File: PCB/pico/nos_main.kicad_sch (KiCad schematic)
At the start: 159 parts, among them U1 PiPico_No_SWD, U2 ADG732BSUZ, U3 DC/DC

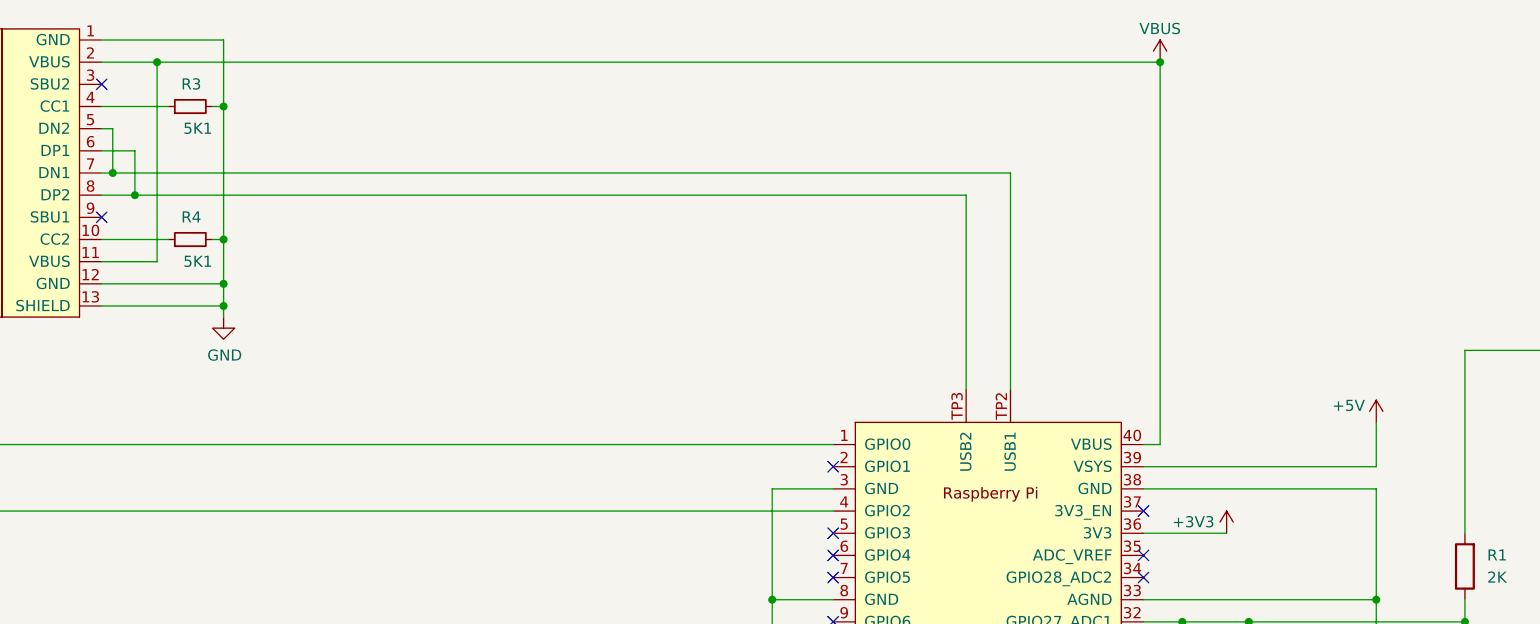
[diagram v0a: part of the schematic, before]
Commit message: Nos Pico PCB v1.12 (isolate vbus)
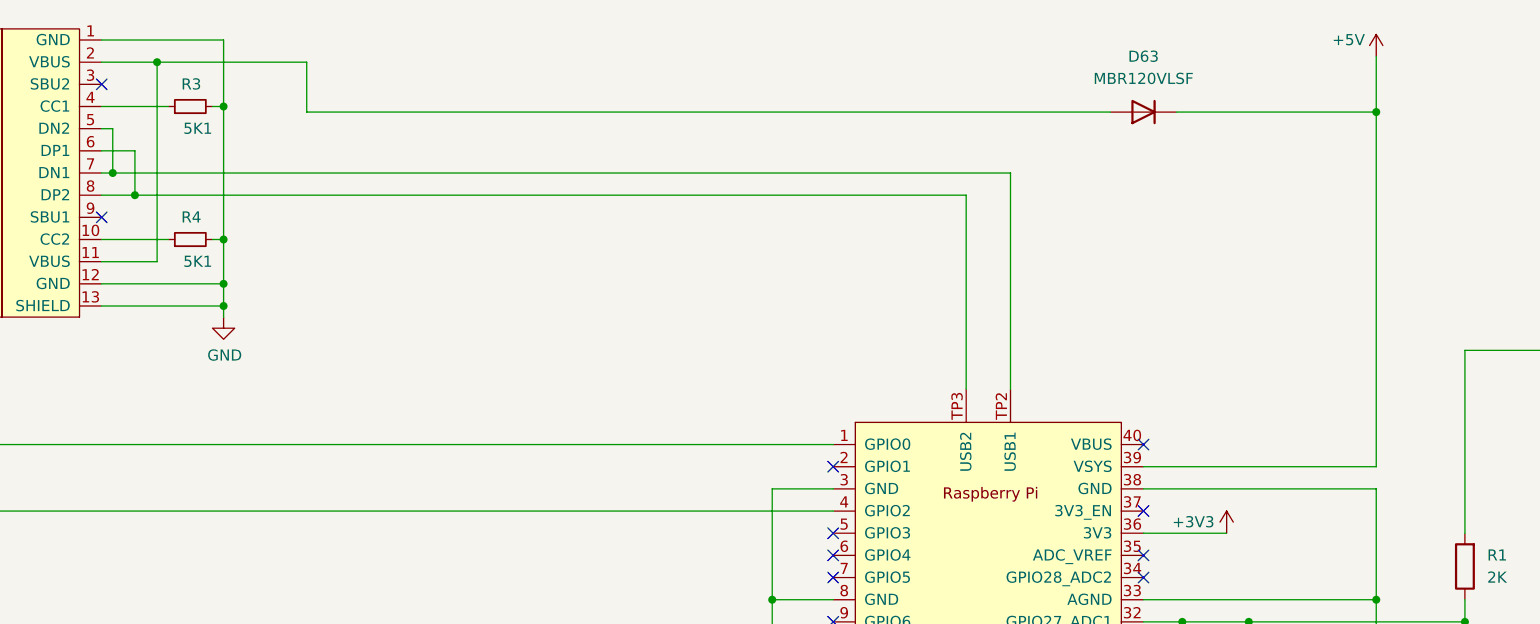
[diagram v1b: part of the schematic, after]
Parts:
- added D63: MBR120VLSF, Diode_SMD:D_SOD-123, symbol Device:D
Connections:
- net +5V: now also D63.1 (K)
- net VBUS: no longer names the net of USB1.11 (VBUS), USB1.2 (VBUS)
- net VBUS: now also D63.2 (A); no longer U1.40 (VBUS)
- no-connect marks 18 -> 19
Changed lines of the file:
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@@
 	)
 	(junction
+		(at 68.58 32.385)
+		(diameter 0)
+		(color 0 0 0 0)
+	)
+	(junction
 		(at 290.195 266.7)
 		(diameter 0)
@@
 	)
 	(junction
+		(at 208.28 38.1)
+		(diameter 0)
+		(color 0 0 0 0)
+	)
+	(junction
 		(at 381 235.585)
 		(diameter 0)
@@
 	)
 	(junction
-		(at 68.58 32.385)
-		(diameter 0)
-		(color 0 0 0 0)
-	)
-	(junction
 		(at 125.095 193.04)
 		(diameter 0)
@@
 	)
 	(junction
-		(at 183.515 32.385)
-		(diameter 0)
-		(color 0 0 0 0)
-	)
-	(junction
 		(at 74.295 215.9)
 		(diameter 0)
@@
 	)
 	(no_connect
+		(at 181.61 76.2)
+	)
+	(no_connect
 		(at 146.05 86.36)
 	)
@@
 	(wire
 		(pts
-			(xy 68.58 32.385) (xy 183.515 32.385)
-		)
-		(stroke
-			(width 0)
-			(type default)
-		)
-	)
-	(wire
-		(pts
 			(xy 407.035 266.7) (xy 419.735 266.7)
 		)
@@
 	(wire
 		(pts
+			(xy 208.28 38.1) (xy 208.28 78.74)
+		)
+		(stroke
+			(width 0)
+			(type default)
+		)
+	)
+	(wire
+		(pts
 			(xy 48.895 215.9) (xy 61.595 215.9)
 		)
@@
 	(wire
 		(pts
-			(xy 183.515 32.385) (xy 183.515 76.2)
-		)
-		(stroke
-			(width 0)
-			(type default)
-		)
-	)
-	(wire
-		(pts
 			(xy 137.795 165.735) (xy 150.495 165.735)
 		)
@@
 	(wire
 		(pts
-			(xy 208.28 73.66) (xy 208.28 78.74)
+			(xy 208.28 31.75) (xy 208.28 38.1)
 		)
 		(stroke
@@
 	(wire
 		(pts
-			(xy 400.05 235.585) (xy 413.385 235.585)
+			(xy 177.8 38.1) (xy 85.725 38.1)
 		)
 		(stroke
@@
 	(wire
 		(pts
-			(xy 353.695 266.7) (xy 368.935 266.7)
+			(xy 400.05 235.585) (xy 413.385 235.585)
 		)
 		(stroke
@@
 	(wire
 		(pts
-			(xy 381 235.585) (xy 400.05 235.585)
+			(xy 353.695 266.7) (xy 368.935 266.7)
 		)
 		(stroke
@@
 	(wire
 		(pts
-			(xy 62.23 40.005) (xy 63.5 40.005)
+			(xy 381 235.585) (xy 400.05 235.585)
 		)
 		(stroke
@@
 	(wire
 		(pts
-			(xy 290.195 266.7) (xy 302.895 266.7)
+			(xy 62.23 40.005) (xy 63.5 40.005)
 		)
 		(stroke
@@
 	(wire
 		(pts
-			(xy 201.295 193.04) (xy 213.995 193.04)
+			(xy 290.195 266.7) (xy 302.895 266.7)
 		)
 		(stroke
@@
 	(wire
 		(pts
-			(xy 170.18 296.545) (xy 182.88 296.545)
+			(xy 201.295 193.04) (xy 213.995 193.04)
 		)
 		(stroke
@@
 	(wire
 		(pts
-			(xy 183.515 76.2) (xy 181.61 76.2)
+			(xy 170.18 296.545) (xy 182.88 296.545)
 		)
 		(stroke
@@
 	(wire
 		(pts
+			(xy 85.725 38.1) (xy 85.725 32.385)
+		)
+		(stroke
+			(width 0)
+			(type default)
+		)
+	)
+	(wire
+		(pts
 			(xy 61.595 231.14) (xy 74.295 231.14)
 		)
@@
 	(wire
 		(pts
+			(xy 85.725 32.385) (xy 68.58 32.385)
+		)
+		(stroke
+			(width 0)
+			(type default)
+		)
+	)
+	(wire
+		(pts
 			(xy 323.215 41.91) (xy 325.755 41.91)
 		)
@@
 	(wire
 		(pts
+			(xy 185.42 38.1) (xy 208.28 38.1)
+		)
+		(stroke
+			(width 0)
+			(type default)
+		)
+	)
+	(wire
+		(pts
 			(xy 175.895 208.28) (xy 188.595 208.28)
 		)
@@
 	(symbol
 		(lib_id "power:+5V")
-		(at 208.28 73.66 0)
+		(at 208.28 31.75 0)
 		(unit 1)
 		(exclude_from_sim no)
@@
 		(dnp no)
 		(property "Reference" "#PWR01"
-			(at 208.28 77.47 0)
+			(at 208.28 35.56 0)
 			(effects
 				(font
@@
 		)
 		(property "Value" "+5V"
-			(at 205.105 71.755 0)
+			(at 205.105 29.845 0)
 			(effects
 				(font
@@
 		)
 		(property "Footprint" ""
-			(at 208.28 73.66 0)
+			(at 208.28 31.75 0)
 			(effects
 				(font
@@
 		)
 		(property "Datasheet" ""
-			(at 208.28 73.66 0)
+			(at 208.28 31.75 0)
 			(effects
 				(font
@@
 		)
 		(property "Description" "Power symbol creates a global label with name \"+5V\""
-			(at 208.28 73.66 0)
+			(at 208.28 31.75 0)
 			(effects
 				(font
@@
 	)
 	(symbol
+		(lib_id "Device:D")
+		(at 181.61 38.1 180)
+		(unit 1)
+		(exclude_from_sim no)
+		(in_bom yes)
+		(on_board yes)
+		(dnp no)
+		(fields_autoplaced yes)
+		(property "Reference" "D63"
+			(at 181.61 31.75 0)
+			(effects
+				(font
+					(size 1.27 1.27)
+				)
+			)
+		)
+		(property "Value" "MBR120VLSF"
+			(at 181.61 34.29 0)
+			(effects
+				(font
+					(size 1.27 1.27)
+				)
+			)
+		)
+		(property "Footprint" "Diode_SMD:D_SOD-123"
+			(at 181.61 38.1 0)
+			(effects
+				(font
+					(size 1.27 1.27)
+				)
+				(hide yes)
+			)
+		)
+		(property "Datasheet" "~"
+			(at 181.61 38.1 0)
+			(effects
+				(font
+					(size 1.27 1.27)
+				)
+				(hide yes)
+			)
+		)
+		(property "Description" "Diode"
+			(at 181.61 38.1 0)
+			(effects
+				(font
+					(size 1.27 1.27)
+				)
+				(hide yes)
+			)
+		)
+		(property "Sim.Device" "D"
+			(at 181.61 38.1 0)
+			(effects
+				(font
+					(size 1.27 1.27)
+				)
+				(hide yes)
+			)
+		)
+		(property "Sim.Pins" "1=K 2=A"
+			(at 181.61 38.1 0)
+			(effects
+				(font
+					(size 1.27 1.27)
+				)
+				(hide yes)
+			)
+		)
+		(pin "2"
+		)
+		(pin "1"
+		)
+		(instances
+			(project ""
+				(path "/2e3f5573-c264-4a8b-a2f0-0e6473d39aad"
+					(reference "D63")
+					(unit 1)
+				)
+			)
+		)
+	)
+	(symbol
 		(lib_id "nos_main:WS2812B_Unified")
 		(at 112.395 251.46 0)
@@
 					(unit 1)
 				)
-			)
-		)
-	)
-	(symbol
-		(lib_id "power:+5V")
-		(at 183.515 32.385 0)
-		(unit 1)
-		(exclude_from_sim no)
-		(in_bom yes)
-		(on_board yes)
-		(dnp no)
-		(property "Reference" "#PWR0120"
-			(at 183.515 36.195 0)
-			(effects
-				(font
-					(size 1.27 1.27)
-				)
-				(hide yes)
-			)
-		)
-		(property "Value" "VBUS"
-			(at 183.515 28.575 0)
-			(effects
-				(font
-					(size 1.27 1.27)
-				)
-			)
-		)
-		(property "Footprint" ""
-			(at 183.515 32.385 0)
-			(effects
-				(font
-					(size 1.27 1.27)
-				)
-				(hide yes)
-			)
-		)
-		(property "Datasheet" ""
-			(at 183.515 32.385 0)
-			(effects
-				(font
-					(size 1.27 1.27)
-				)
-				(hide yes)
-			)
-		)
-		(property "Description" ""
-			(at 183.515 32.385 0)
-			(effects
-				(font
-					(size 1.27 1.27)
-				)
-				(hide yes)
-			)
-		)
-		(pin "1"
-		)
-		(instances
-			(project "nos_main"
-				(path "/2e3f5573-c264-4a8b-a2f0-0e6473d39aad"
-					(reference "#PWR0120")
-					(unit 1)
-				)

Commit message: PCB project update
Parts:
- added SW1, SW2, SW3, SW4: SW_SPST, nos_main:SW_SKHHANA010_Combo, symbol Switch:SW_SPST
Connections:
- net GND: now also SW1.1 (A), SW2.1 (A), SW3.1 (A), SW4.1 (A)
- net at U1.14 (GPIO10): now also SW4.2 (B)
- net at U1.15 (GPIO11): now also SW3.2 (B)
- net at U1.16 (GPIO12): now also SW2.2 (B)
- net at U1.17 (GPIO13): now also SW1.2 (B)

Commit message: Nos Pico PCB v1.2 (add buttons)
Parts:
- D63: footprint Diode_SMD:D_SOD-123 -> nos_main:D_SOD-123_LONG
- H1, H10, H11, H12, H13, H14, H15, H16, H17, H18, H19, H2, H20, H21, H22, H23, H24, H25, H26, H27, H28, H3, H4, H5, H6, H7, H8, H9: footprint Package_TO_SOT_SMD:SOT-23-3 -> nos_main:SOT-23-FAT
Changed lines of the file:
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@@
 			)
 		)
-		(property "Footprint" "Package_TO_SOT_SMD:SOT-23-3"
+		(property "Footprint" "nos_main:SOT-23-FAT"
 			(at 383.54 187.325 0)
 			(effects
@@
 			)
 		)
-		(property "Footprint" "Package_TO_SOT_SMD:SOT-23-3"
+		(property "Footprint" "nos_main:SOT-23-FAT"
 			(at 288.29 161.925 0)
 			(effects
@@
 			)
 		)
-		(property "Footprint" "Package_TO_SOT_SMD:SOT-23-3"
+		(property "Footprint" "nos_main:SOT-23-FAT"
 			(at 307.34 161.925 0)
 			(effects
@@
 			)
 		)
-		(property "Footprint" "Package_TO_SOT_SMD:SOT-23-3"
+		(property "Footprint" "nos_main:SOT-23-FAT"
 			(at 402.59 212.725 0)
 			(effects
@@
 			)
 		)
-		(property "Footprint" "Package_TO_SOT_SMD:SOT-23-3"
+		(property "Footprint" "nos_main:SOT-23-FAT"
 			(at 364.49 238.125 0)
 			(effects
@@
 			)
 		)
-		(property "Footprint" "Package_TO_SOT_SMD:SOT-23-3"
+		(property "Footprint" "nos_main:SOT-23-FAT"
 			(at 288.29 238.125 0)
 			(effects
@@
 			)
 		)
-		(property "Footprint" "Package_TO_SOT_SMD:SOT-23-3"
+		(property "Footprint" "nos_main:SOT-23-FAT"
 			(at 307.34 187.325 0)
 			(effects
@@
 			)
 		)
-		(property "Footprint" "Package_TO_SOT_SMD:SOT-23-3"
+		(property "Footprint" "nos_main:SOT-23-FAT"
 			(at 402.59 187.325 0)
 			(effects
@@
 			)
 		)
-		(property "Footprint" "Package_TO_SOT_SMD:SOT-23-3"
+		(property "Footprint" "nos_main:SOT-23-FAT"
 			(at 288.29 212.725 0)
 			(effects
@@
 			)
 		)
-		(property "Footprint" "Package_TO_SOT_SMD:SOT-23-3"
+		(property "Footprint" "nos_main:SOT-23-FAT"
 			(at 364.49 212.725 0)
 			(effects
@@
 			)
 		)
-		(property "Footprint" "Package_TO_SOT_SMD:SOT-23-3"
+		(property "Footprint" "nos_main:SOT-23-FAT"
 			(at 345.44 212.725 0)
 			(effects
@@
 			)
 		)
-		(property "Footprint" "Package_TO_SOT_SMD:SOT-23-3"
+		(property "Footprint" "nos_main:SOT-23-FAT"
 			(at 402.59 238.125 0)
 			(effects
@@
 			)
 		)
-		(property "Footprint" "Package_TO_SOT_SMD:SOT-23-3"
+		(property "Footprint" "nos_main:SOT-23-FAT"
 			(at 307.34 238.125 0)
 			(effects
@@
 			)
 		)
-		(property "Footprint" "Package_TO_SOT_SMD:SOT-23-3"
+		(property "Footprint" "nos_main:SOT-23-FAT"
 			(at 326.39 238.125 0)
 			(effects
@@
 			)
 		)
-		(property "Footprint" "Package_TO_SOT_SMD:SOT-23-3"
+		(property "Footprint" "nos_main:SOT-23-FAT"
 			(at 345.44 161.925 0)
 			(effects
@@
 			)
 		)
-		(property "Footprint" "Package_TO_SOT_SMD:SOT-23-3"
+		(property "Footprint" "nos_main:SOT-23-FAT"
 			(at 288.29 187.325 0)
 			(effects
@@
 			)
 		)
-		(property "Footprint" "Package_TO_SOT_SMD:SOT-23-3"
+		(property "Footprint" "nos_main:SOT-23-FAT"
 			(at 383.54 161.925 0)
 			(effects
@@
 			)
 		)
-		(property "Footprint" "Package_TO_SOT_SMD:SOT-23-3"
+		(property "Footprint" "nos_main:SOT-23-FAT"
 			(at 364.49 161.925 0)
 			(effects
@@
 			)
 		)
-		(property "Footprint" "Package_TO_SOT_SMD:SOT-23-3"
+		(property "Footprint" "nos_main:SOT-23-FAT"
 			(at 326.39 161.925 0)
 			(effects
@@
 			)
 		)
-		(property "Footprint" "Package_TO_SOT_SMD:SOT-23-3"
+		(property "Footprint" "nos_main:SOT-23-FAT"
 			(at 326.39 212.725 0)
 			(effects
@@
 			)
 		)
-		(property "Footprint" "Package_TO_SOT_SMD:SOT-23-3"
+		(property "Footprint" "nos_main:SOT-23-FAT"
 			(at 326.39 187.325 0)
 			(effects
@@
 			)
 		)
-		(property "Footprint" "Package_TO_SOT_SMD:SOT-23-3"
+		(property "Footprint" "nos_main:SOT-23-FAT"
 			(at 364.49 187.325 0)
 			(effects
@@
 			)
 		)
-		(property "Footprint" "Package_TO_SOT_SMD:SOT-23-3"
+		(property "Footprint" "nos_main:SOT-23-FAT"
 			(at 345.44 238.125 0)
 			(effects
@@
 			)
 		)
-		(property "Footprint" "Diode_SMD:D_SOD-123"
+		(property "Footprint" "nos_main:D_SOD-123_LONG"
 			(at 181.61 38.1 0)
 			(effects
@@
 			)
 		)
-		(property "Footprint" "Package_TO_SOT_SMD:SOT-23-3"
+		(property "Footprint" "nos_main:SOT-23-FAT"
 			(at 402.59 161.925 0)
 			(effects
@@
 			)
 		)
-		(property "Footprint" "Package_TO_SOT_SMD:SOT-23-3"
+		(property "Footprint" "nos_main:SOT-23-FAT"
 			(at 383.54 212.725 0)
 			(effects
@@
 			)
 		)
-		(property "Footprint" "Package_TO_SOT_SMD:SOT-23-3"
+		(property "Footprint" "nos_main:SOT-23-FAT"
 			(at 383.54 238.125 0)
 			(effects
@@
 			)
 		)
-		(property "Footprint" "Package_TO_SOT_SMD:SOT-23-3"
+		(property "Footprint" "nos_main:SOT-23-FAT"
 			(at 307.34 212.725 0)
 			(effects
@@
 			)
 		)
-		(property "Footprint" "Package_TO_SOT_SMD:SOT-23-3"
+		(property "Footprint" "nos_main:SOT-23-FAT"
 			(at 345.44 187.325 0)
 			(effects
